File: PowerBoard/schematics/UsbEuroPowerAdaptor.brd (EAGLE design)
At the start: 69.5 x 100 mm, 21 parts, among them IC1 TEC-2SIP, IC2 TBA-2SIP, J1 POWER_JACK, U4 REG_S9V11F5

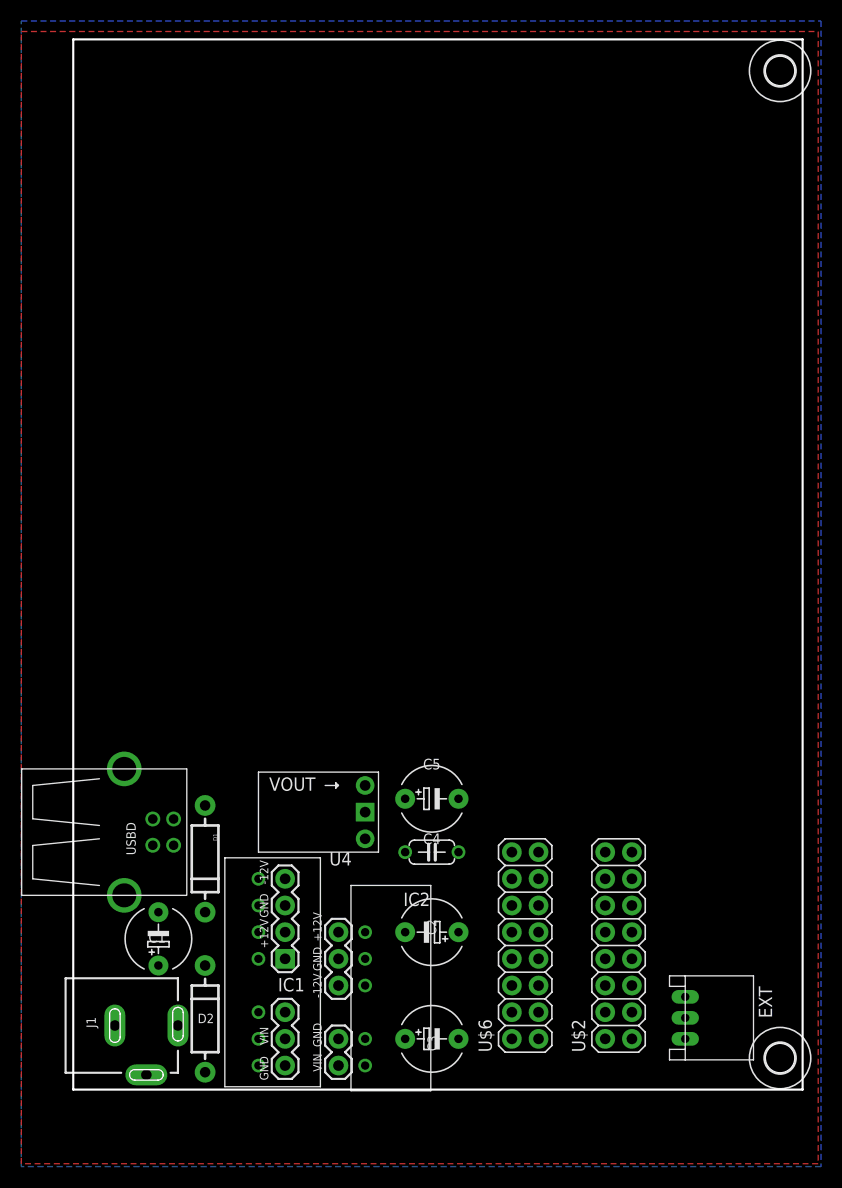
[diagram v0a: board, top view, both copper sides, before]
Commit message: added dc converter parts
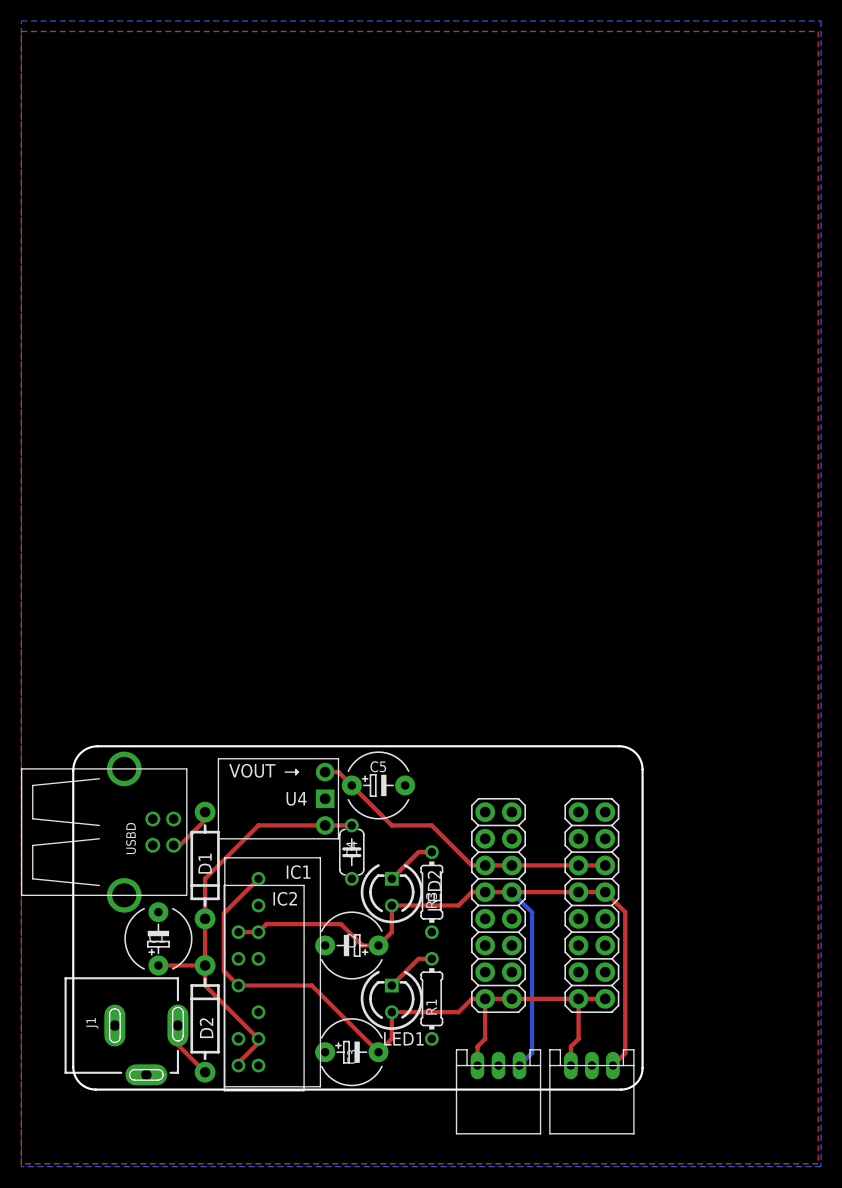
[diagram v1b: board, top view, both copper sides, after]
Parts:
- removed JP1: (no value), SparkFun:1X02
- removed JP2, JP4: (no value), SparkFun:1X03
- removed JP3: (no value), SparkFun:1X04
- removed U$1, U$5: (no value), holes:2,8
- added EXT1: CON-JST_PH_3W, Rebel:CON-JST_PH_3W
- added LED1, LED2: (no value), Rebel:LED3MM
- added R1, R3: 2k, Rebel:0204/7
- moved IC2 12.1 mm to (15.9, 2.54)
- moved EXT 11.2 mm to (47.5, 2.54), turned to 180 degrees
- moved C3 7.73 mm to (26.7, 3.81)
- moved C2 7.73 mm to (26.7, 14.0)
- moved C4 7.62 mm to (26.7, 22.9), turned to 270 degrees
- moved C5 5.24 mm to (29.2, 29.2)
- moved U$2 4.58 mm to (50.8, 8.89)
- moved U$6 4.58 mm to (41.9, 8.89)
- moved U4 4.02 mm to (24.1, 27.9)
- moved D1 0.64 mm to (12.7, 21.6)
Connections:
- new net N$1: LED2.K, R3.2
- new net N$2: LED1.K, R1.2
- net +12V: now also EXT1.P3, LED2.A; no longer JP3.2, JP4.3
- net +9V: no longer JP1.1, JP2.2
- net -12V: now also EXT1.P1, LED1.A; no longer JP3.4, JP4.1
- net GND: now also EXT1.P2, R1.1, R3.1; no longer JP1.2, JP2.1, JP3.3, JP4.2
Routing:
- net +12V: track 0.00 -> 75.3 mm
- net -12V: track 0.00 -> 66.6 mm
- net +9V: track 0.00 -> 41.2 mm
- net +5V: track 0.00 -> 30.4 mm
- net N$9: track 0.00 -> 5.52 mm
- net N$2: track 0.00 -> 4.86 mm
- net N$1: track 0.00 -> 4.86 mm
- net EXT_USB_D_VBUS: track 0.00 -> 4.75 mm
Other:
- board size 69.5 x 100 mm -> 54.2 x 32.7 mm
- board text added: "USB Euro Power Rev01"
- board text removed: "+12V"
- board text removed: "-12V"
- board text removed: "GND"
- board text removed: "Magus Connectors Rev07"
- board text removed: "VIN"

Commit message: USB power adaptor Rev01
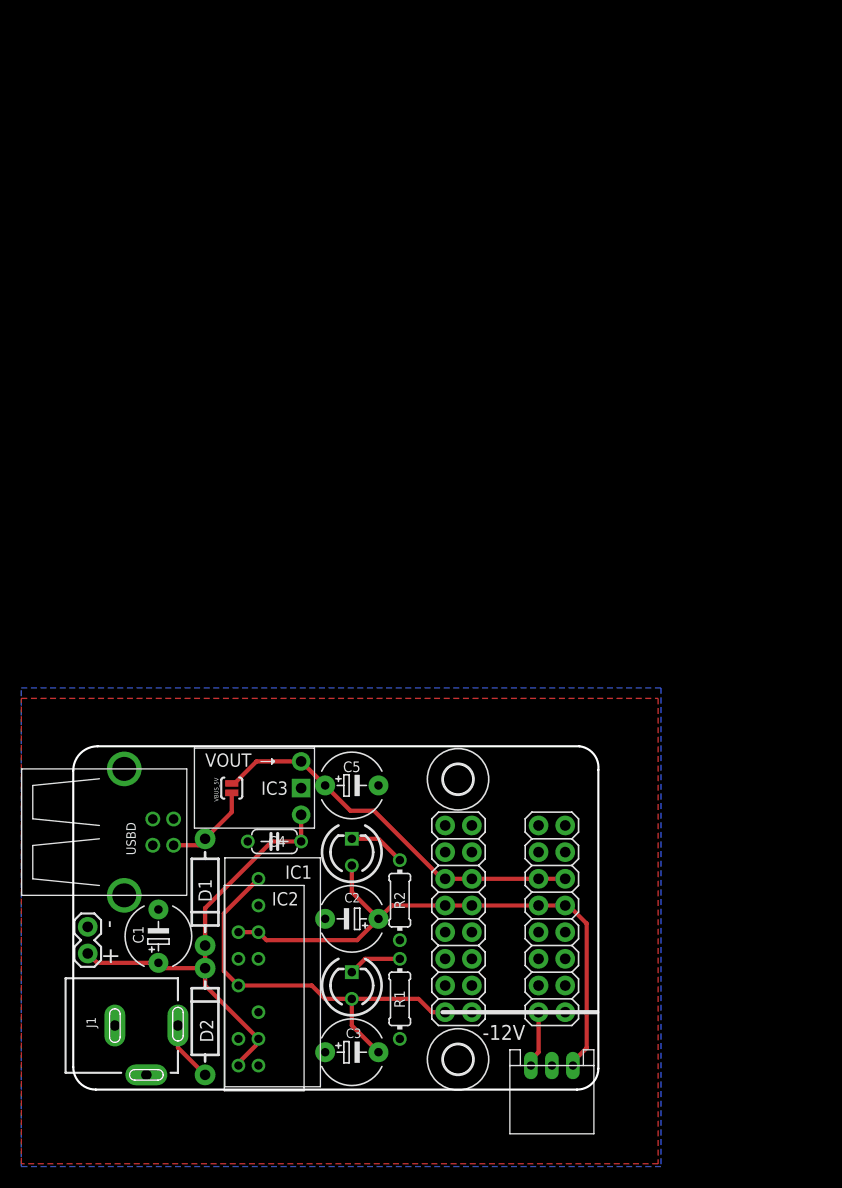
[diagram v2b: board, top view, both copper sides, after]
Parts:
- removed EXT1: CON-JST_PH_3W, Rebel:CON-JST_PH_3W
- removed R3: 2k, Rebel:0204/7
- removed U4: REG_S9V11F5, Rebel:REG_S9V11F5
- added IC3: REG_S9V11F5, Rebel:REG_S9V11F5
- added JP1: (no value), SparkFun:1X02
- added R2: 2k, Rebel:0204/7
- added U$1, U$3: (no value), holes:2,8
- added VBUS_5V: SOLDERJUMPERNO, SparkFun:SJ_2S-NO
- C1: value 100u 16v -> 47u
- C2, C3: value 47u 16v -> 47u
- D1: value SL04 -> 1N5817
- D2: value SL04 -> 1N4001
- moved C4 7.44 mm to (19.3, 23.9), turned to 180 degrees
- moved LED2 5.39 mm to (26.7, 22.9)
- moved LED1 4.02 mm to (26.7, 10.2)
- moved U$2 4.02 mm to (47.0, 7.62)
- moved U$6 4.02 mm to (38.1, 7.62)
- moved EXT 3.81 mm to (43.7, 2.54)
- moved R1 3.05 mm to (31.2, 8.89)
- moved C2 2.54 mm to (26.7, 16.5)
- moved C5 2.54 mm to (26.7, 29.2)
- moved D1 2.54 mm to (12.7, 19.1)
- moved D2 0.25 mm to (12.7, 6.73)
- moved C1 0.25 mm to (8.26, 14.9)
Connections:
- net +12V: no longer EXT1.P3
- net +5V: now also IC3.VOUT, VBUS_5V.2; no longer U4.VOUT
- net +9V: now also IC3.VIN, JP1.2; no longer U4.VIN
- net -12V: no longer EXT1.P1
- net EXT_USB_D_VBUS: now also VBUS_5V.1
- net GND: now also IC3.GND, JP1.1, R2.1; no longer EXT1.P2, R3.1, U4.GND
- net N$1: now also R2.2; no longer R3.2
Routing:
- net +12V: track 75.3 -> 55.7 mm
- net -12V: track 66.6 -> 55.8 mm
- net +5V: track 30.4 -> 37.2 mm
- net EXT_USB_D_VBUS: track 4.75 -> 8.68 mm
- net +9V: track 41.2 -> 43.9 mm
- net N$1: track 4.86 -> 5.41 mm
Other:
- board size 54.2 x 32.7 mm -> 50 x 32.7 mm
- board text added: "+"
- board text added: "-"
- board text added: "-12V"
- board text added: "GND"
- board text added: "VIN"

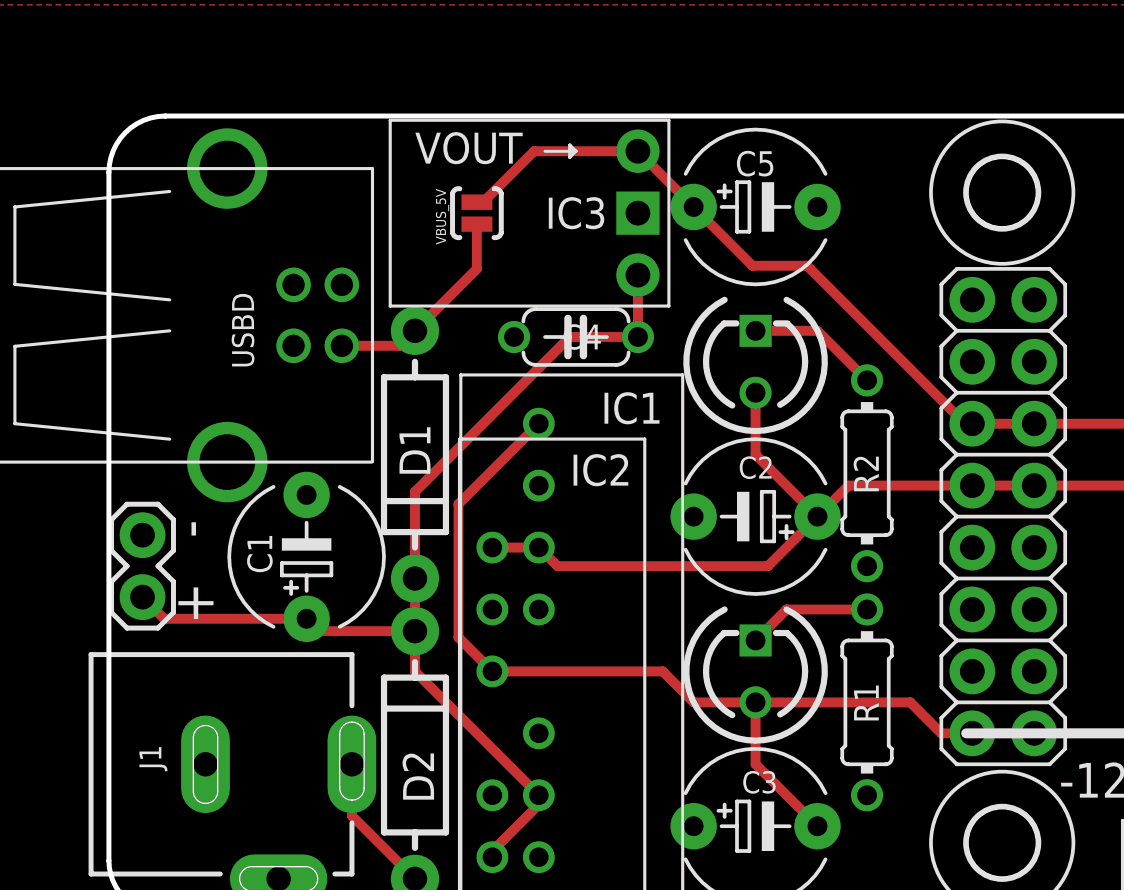
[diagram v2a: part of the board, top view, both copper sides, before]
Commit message: Rotated leds. Changed label to Rev02
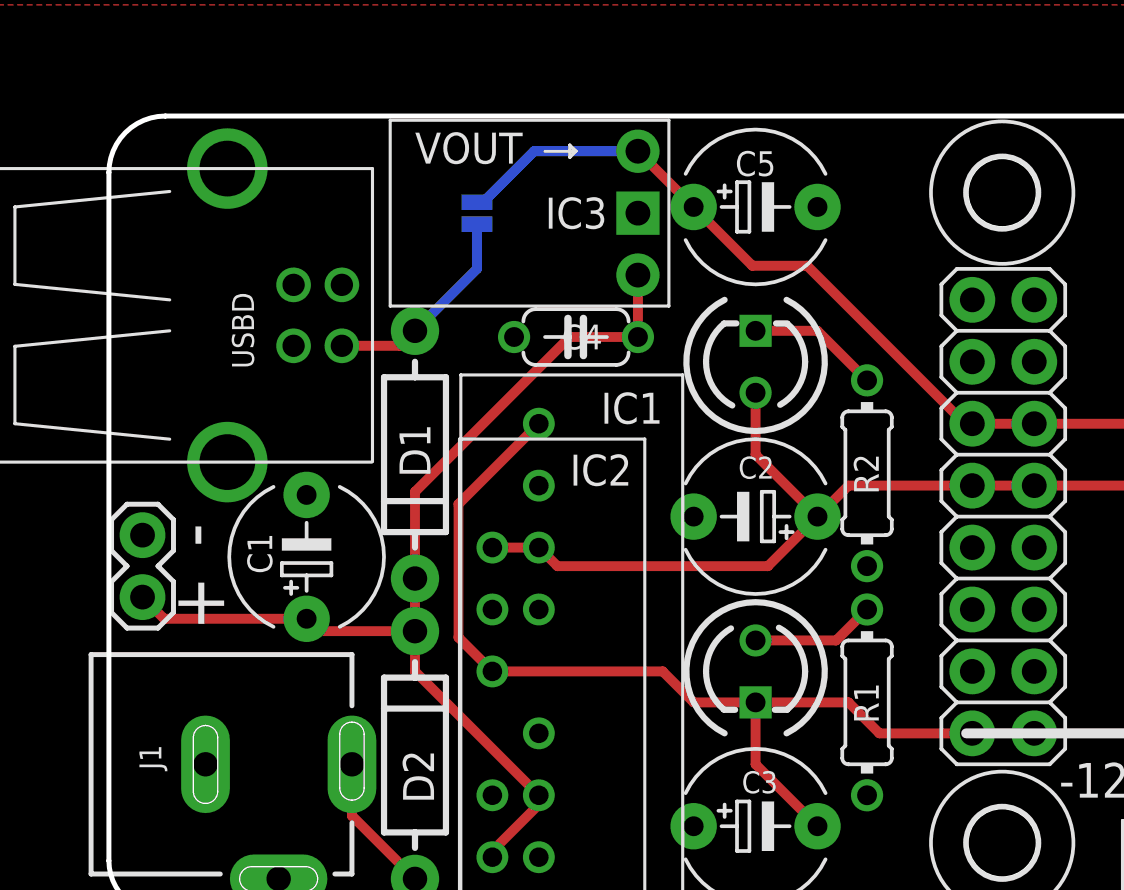
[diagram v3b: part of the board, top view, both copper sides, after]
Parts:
- turned LED1 to 270 degrees
- flipped VBUS_5V to the bottom
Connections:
- net -12V: now also LED1.K; no longer LED1.A
- net N$2: now also LED1.A; no longer LED1.K
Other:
- board text added: "USB Euro Power Rev02"
- board text removed: "USB Euro Power Rev01"
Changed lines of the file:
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@@
 <drawing>
 <settings>
-<setting alwaysvectorfont="yes"/>
+<setting alwaysvectorfont="no"/>
 <setting keepoldvectorfont="yes"/>
 <setting verticaltext="up"/>
@@
 <wire x1="0.145" y1="30.625" x2="2.46" y2="32.94" width="0.204" layer="20" curve="-90"/>
 <text x="32.483" y="4.711" size="1.778" layer="22" font="vector" rot="MR90">Rebel Technology</text>
-<text x="18.836" y="0.888" size="1.778" layer="22" font="vector" rot="MR90">USB Euro Power Rev01</text>
+<text x="18.836" y="0.888" size="1.778" layer="22" font="vector" rot="MR90">USB Euro Power Rev02</text>
 <dimension x1="0.145" y1="0.25" x2="50.145" y2="0.21" x3="25.142765625" y3="-2.56" textsize="1.4224" layer="47"/>
 <text x="2.667" y="10.668" size="1.778" layer="22" font="vector" rot="MR270">9V DC</text>
@@
 <text x="2.994" y="16.006" size="1.016" layer="22" font="vector" rot="MR90" align="bottom-center">GND</text>
 <text x="2.994" y="12.958" size="1.016" layer="22" font="vector" rot="MR90" align="bottom-center">VIN</text>
-<text x="2.994" y="16.006" size="1.6764" layer="21" font="vector" rot="SR270" align="bottom-center">-</text>
-<text x="2.994" y="12.958" size="1.6764" layer="21" font="vector" rot="SR270" align="bottom-center">+</text>
+<text x="2.994" y="15.752" size="2.1844" layer="21" font="vector" rot="SR270" align="bottom-center">-</text>
+<text x="2.994" y="12.958" size="2.1844" layer="21" font="vector" rot="SR270" align="bottom-center">+</text>
 <wire x1="50.038" y1="7.62" x2="35.306" y2="7.62" width="0.4064" layer="21"/>
 <wire x1="50.038" y1="7.62" x2="35.306" y2="7.62" width="0.4064" layer="22"/>
@@
 <attribute name="VALUE" x="29.9466" y="15.748" size="1.016" layer="27" font="vector" ratio="10" rot="R90"/>
 </element>
-<element name="LED1" library="Rebel" package="LED3MM" value="" x="26.67" y="10.16" smashed="yes" rot="R90">
-<attribute name="VALUE" x="28.321" y="12.065" size="1.27" layer="27" ratio="10" rot="R90"/>
+<element name="LED1" library="Rebel" package="LED3MM" value="" x="26.67" y="10.16" smashed="yes" rot="R270">
+<attribute name="VALUE" x="25.019" y="8.255" size="1.27" layer="27" ratio="10" rot="R270"/>
 </element>
 <element name="R1" library="Rebel" package="0204/7" value="2k" x="31.242" y="8.89" smashed="yes" rot="R90">
@@
 <attribute name="VALUE" x="29.9466" y="6.35" size="1.016" layer="27" font="vector" ratio="10" rot="R90"/>
 </element>
-<element name="VBUS_5V" library="SparkFun" package="SJ_2S-NO" value="SOLDERJUMPERNO" x="15.24" y="28.956" smashed="yes" rot="R90">
-<attribute name="NAME" x="13.97" y="27.667" size="0.4064" layer="25" rot="R90"/>
-<attribute name="VALUE" x="16.891" y="28.048" size="0.4064" layer="27" rot="R90"/>
+<element name="VBUS_5V" library="SparkFun" package="SJ_2S-NO" value="SOLDERJUMPERNO" x="15.24" y="28.956" smashed="yes" rot="MR90">
+<attribute name="NAME" x="16.51" y="27.667" size="0.4064" layer="26" rot="MR90"/>
+<attribute name="VALUE" x="13.589" y="28.048" size="0.4064" layer="28" rot="MR90"/>
 </element>
 <element name="JP1" library="SparkFun" package="1X02" value="" x="1.524" y="15.748" smashed="yes" rot="R270">
@@
 <wire x1="12.7" y1="24.13" x2="12.085" y2="23.515" width="0.4064" layer="1"/>
 <contactref element="VBUS_5V" pad="1"/>
-<wire x1="12.7" y1="24.13" x2="15.24" y2="26.67" width="0.4064" layer="1"/>
-<wire x1="15.24" y1="26.67" x2="15.24" y2="28.506" width="0.4064" layer="1"/>
+<wire x1="12.7" y1="24.13" x2="15.24" y2="26.67" width="0.4064" layer="16"/>
+<wire x1="15.24" y1="26.67" x2="15.24" y2="28.506" width="0.4064" layer="16"/>
 </signal>
 <signal name="GND">
@@
 <wire x1="14.4844" y1="17.0244" x2="14.4844" y2="11.5506" width="0.4064" layer="1"/>
 <wire x1="22.86" y1="10.16" x2="15.875" y2="10.16" width="0.4064" layer="1"/>
-<contactref element="LED1" pad="A"/>
-<wire x1="26.67" y1="8.89" x2="24.13" y2="8.89" width="0.4064" layer="1"/>
-<wire x1="24.13" y1="8.89" x2="22.86" y2="10.16" width="0.4064" layer="1"/>
+<wire x1="22.86" y1="10.16" x2="24.13" y2="8.89" width="0.4064" layer="1"/>
 <wire x1="29.21" y1="3.81" x2="26.67" y2="6.35" width="0.4064" layer="1"/>
+<contactref element="LED1" pad="K"/>
+<wire x1="24.13" y1="8.89" x2="26.67" y2="8.89" width="0.4064" layer="1"/>
 <wire x1="26.67" y1="6.35" x2="26.67" y2="8.89" width="0.4064" layer="1"/>
-<wire x1="26.67" y1="8.89" x2="33.02" y2="8.89" width="0.4064" layer="1"/>
-<wire x1="33.02" y1="8.89" x2="34.29" y2="7.62" width="0.4064" layer="1"/>
-<wire x1="34.29" y1="7.62" x2="35.56" y2="7.62" width="0.4064" layer="1"/>
+<wire x1="31.75" y1="7.62" x2="30.48" y2="8.89" width="0.4064" layer="1"/>
+<wire x1="30.48" y1="8.89" x2="26.67" y2="8.89" width="0.4064" layer="1"/>
+<wire x1="35.56" y1="7.62" x2="31.75" y2="7.62" width="0.4064" layer="1"/>
 </signal>
 <signal name="+9V">
@@
 <wire x1="44.45" y1="20.32" x2="46.99" y2="20.32" width="0.4064" layer="1"/>
 <contactref element="VBUS_5V" pad="2"/>
-<wire x1="15.24" y1="29.406" x2="15.494" y2="29.406" width="0.4064" layer="1"/>
-<wire x1="17.584" y1="31.496" x2="15.494" y2="29.406" width="0.4064" layer="1"/>
-<wire x1="17.584" y1="31.496" x2="21.844" y2="31.496" width="0.4064" layer="1"/>
+<wire x1="15.24" y1="29.406" x2="15.494" y2="29.406" width="0.4064" layer="16"/>
+<wire x1="17.584" y1="31.496" x2="15.494" y2="29.406" width="0.4064" layer="16"/>
+<wire x1="17.584" y1="31.496" x2="21.844" y2="31.496" width="0.4064" layer="16"/>
 </signal>
 <signal name="N$1">
@@
 </signal>
 <signal name="N$2">
-<contactref element="LED1" pad="K"/>
 <contactref element="R1" pad="2"/>
-<wire x1="26.67" y1="11.43" x2="27.94" y2="12.7" width="0.4064" layer="1"/>
-<wire x1="27.94" y1="12.7" x2="31.242" y2="12.7" width="0.4064" layer="1"/>
+<contactref element="LED1" pad="A"/>
+<wire x1="31.242" y1="12.7" x2="29.972" y2="11.43" width="0.4064" layer="1"/>
+<wire x1="29.972" y1="11.43" x2="26.67" y2="11.43" width="0.4064" layer="1"/>
 </signal>
 </signals>
